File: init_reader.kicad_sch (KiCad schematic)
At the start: 3 parts, among them U1 LCD_16x4, U2 MAX232

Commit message: update schematics
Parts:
- added BT1: Battery, Battery:BatteryHolder_MPD_BA9VPC_1xPP3, symbol Device:Battery
- added C1, C2, C3, C4: 10uF, Capacitor_THT:CP_Radial_D5.0mm_P2.50mm, symbol Device:C_Polarized
- added J1: DE9_Pins, Connector_Dsub:DSUB-9_Pins_Horizontal_P2.77x2.54mm_EdgePinOffset9.40mm, symbol Connector:DE9_Pins
- added R1: R, Resistor_THT:R_Axial_DIN0207_L6.3mm_D2.5mm_P7.62mm_Horizontal, symbol Device:R
- U1: footprint PCM_SL_Breakout_Boards:LCD-16X4 -> 0_moje:AC-164A
- U2: footprint (none) -> Package_DIP:DIP-16_W7.62mm
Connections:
- net +5V: now also U1.15 (LED_A), U1.2 (VDD), U2.16 (VCC), C3.2
- net GND: now also A1.13 (GND), A1.18 (GND), A1.23 (GND), A1.28 (GND), A1.3 (GND), A1.38 (GND), A1.8 (GND), U1.1 (VSS), U1.16 (LED_K), U1.5 (RW), U2.15 (GND), C4.1, J1.5, R1.2
- net DB4: now reaches U1.11 (DB4)
- net DB4: now also A1.25 (GPIO19)
- net DB5: now reaches U1.12 (DB5)
- net DB5: now also A1.24 (GPIO18)
- net DB6: now reaches U1.13 (DB6)
- net DB6: now also A1.22 (GPIO17)
- net DB7: now reaches U1.14 (DB7)
- net DB7: now also A1.21 (GPIO16)
- net at U1.3 (VO): now also R1.1
- net RS: now reaches U1.4 (RS)
- net RS: now also A1.27 (GPIO21)
- net En: now reaches U1.6 (E)
- net En: now also A1.26 (GPIO20)
- net at U2.1 (C1+): now also C1.1
- net T1OUT: now reaches U2.11 (T1IN)
- net R1OUT: now reaches U2.12 (R1OUT)
- net R1IN: now reaches U2.13 (R1IN)
- net R1IN: now also J1.3
- net T1IN: now reaches U2.14 (T1OUT)
- net T1IN: now also J1.2
- net at U2.2 (VS+): now also C3.1
- net at U2.3 (C1-): now also C1.2
- net at U2.4 (C2+): now also C2.1
- net at U2.5 (C2-): now also C2.2
- net at U2.6 (VS-): now also C4.2
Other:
- moved on the sheet: U1

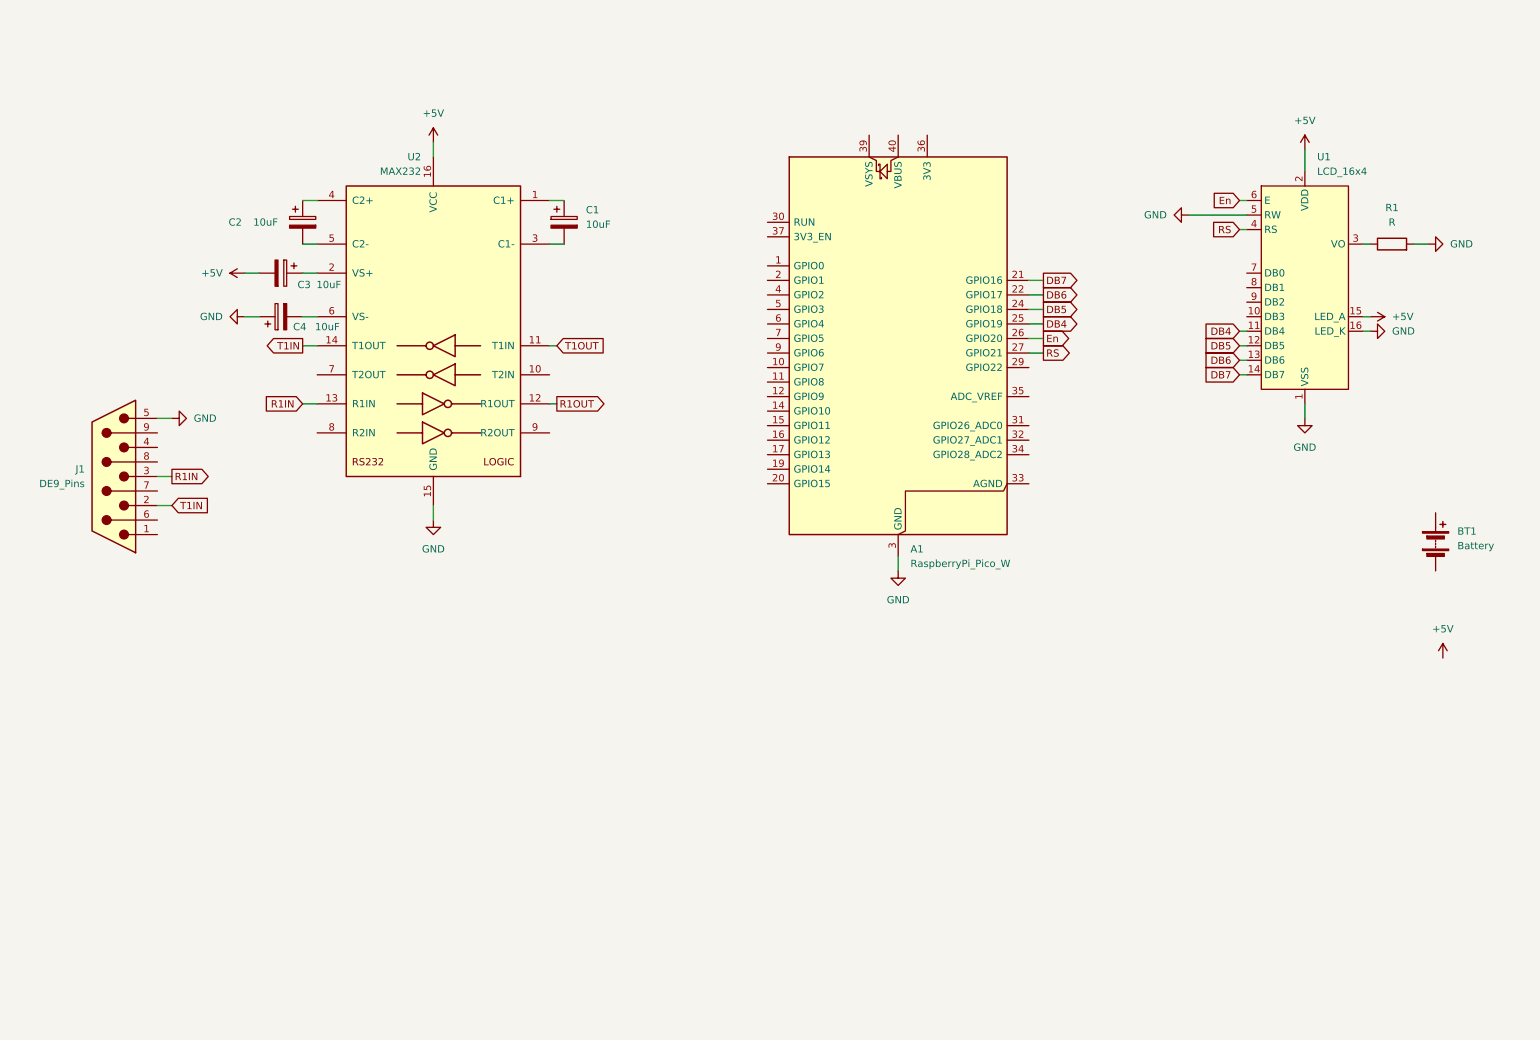
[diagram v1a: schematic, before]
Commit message: add all components - basic circuit
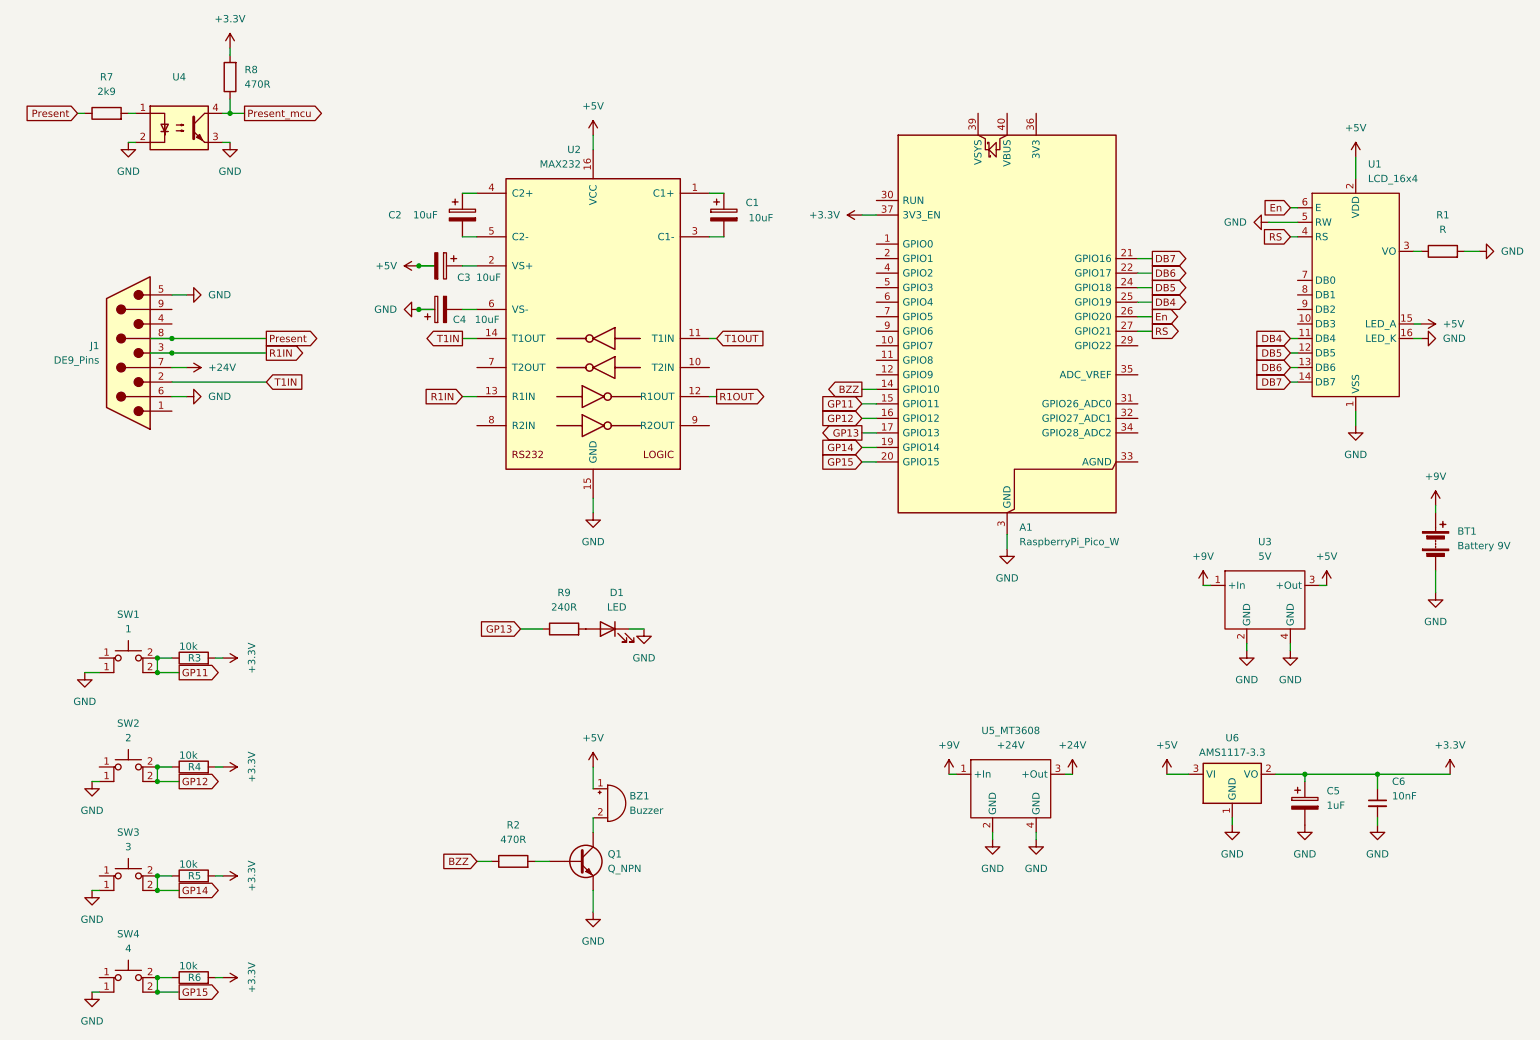
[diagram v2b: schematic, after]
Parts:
- added BZ1: Buzzer, Buzzer_Beeper:Buzzer_12x9.5RM7.6, symbol 00_my_basic:Buzzer
- added C5: 1uF, Capacitor_THT:CP_Radial_D5.0mm_P2.50mm, symbol Device:C_Polarized
- added C6: 10nF, PCM_SparkFun-Capacitor:C_0603_1608Metric, symbol 00_my_basic:C
- added D1: LED, LED_THT:LED_D3.0mm, symbol Device:LED
- added Q1: Q_NPN, Package_TO_SOT_THT:TO-92_Inline, symbol 00_my_basic:Q_NPN
- added R2, R8: 470R, Resistor_THT:R_Axial_DIN0207_L6.3mm_D2.5mm_P7.62mm_Horizontal, symbol Device:R
- added R3, R4, R5, R6: 10k, Resistor_THT:R_Axial_DIN0207_L6.3mm_D2.5mm_P7.62mm_Horizontal, symbol Device:R
- added R7: 2k9, Resistor_THT:R_Axial_DIN0207_L6.3mm_D2.5mm_P7.62mm_Horizontal, symbol Device:R
- added R9: 240R, Resistor_THT:R_Axial_DIN0207_L6.3mm_D2.5mm_P7.62mm_Horizontal, symbol Device:R
- added SW1: 1, Button_Switch_THT:SW_TH_Tactile_Omron_B3F-100x, symbol 00_my_basic:Switch 4 poly
- added SW2: 2, Button_Switch_THT:SW_TH_Tactile_Omron_B3F-100x, symbol 00_my_basic:Switch 4 poly
- added SW3: 3, Button_Switch_THT:SW_TH_Tactile_Omron_B3F-100x, symbol 00_my_basic:Switch 4 poly
- added SW4: 4, Button_Switch_THT:SW_TH_Tactile_Omron_B3F-100x, symbol 00_my_basic:Switch 4 poly
- added U3: 5V, 00_dc_dc:dc-dc-HW613, symbol 00_my_basic:DC/DC
- added U4: Optocoupler_DC_PhotoNPN_AKEC, OptoDevice:Vishay_CNY70, symbol Isolator:Optocoupler_DC_PhotoNPN_AKEC
- added U5_MT3608: +24V, 00_dc_dc:dc_dc_MT3608, symbol 00_my_basic:DC/DC
- added U6: AMS1117-3.3, Package_TO_SOT_SMD:SOT-223-3_TabPin2, symbol Regulator_Linear:AMS1117-3.3
- A1: footprint Module:RaspberryPi_Pico_W_SMD_HandSolder -> 00_ruzne:RaspberryPi_Pico_Common_THT
- BT1: value Battery -> Battery 9V
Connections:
- net +5V: now also BZ1.1 (+), U3.3 (+Out), U6.3 (VI)
- net GND: now also BT1.2 (-), J1.6, C5.2, C6.2, D1.1 (K), Q1.3 (E), SW1.1, SW2.1, SW3.1, SW4.1, U3.2 (GND), U3.4 (GND), U4.2, U4.3, U5_MT3608.2 (GND), U5_MT3608.4 (GND), U6.1 (GND)
- net +9V: now reaches BT1.1 (+)
- net +9V: now also U3.1 (+In), U5_MT3608.1 (+In)
- net +24V: now reaches J1.7
- net +24V: now also U5_MT3608.3 (+Out)
- net Present: now reaches J1.8
- net Present: now also R7.1
- net BZZ: now reaches A1.14 (GPIO10)
- net BZZ: now also R2.1
- net GP11: now reaches A1.15 (GPIO11)
- net GP11: now also R3.1, SW1.2
- net GP12: now reaches A1.16 (GPIO12)
- net GP12: now also R4.1, SW2.2
- net GP13: now reaches A1.17 (GPIO13)
- net GP13: now also R9.1
- net GP14: now reaches A1.19 (GPIO14)
- net GP14: now also R5.1, SW3.2
- net GP15: now reaches A1.20 (GPIO15)
- net GP15: now also R6.1, SW4.2
- net +3.3V: now reaches A1.37 (3V3_EN)
- net +3.3V: now also C5.1, C6.1, R3.2, R4.2, R5.2, R6.2, R8.2, U6.2 (VO)
- new net: Q1.2 (B), R2.2
- new net: R7.2, U4.1
- new net: D1.2 (A), R9.2
- new net: BZ1.2 (-), Q1.1 (C)
- new net Present_mcu: R8.1, U4.4
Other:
- moved on the sheet: A1, C1, C2, C3, C4, J1, R1, U1, U2

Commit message: update all
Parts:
- U4: footprint OptoDevice:Vishay_CNY70 -> Package_DIP:DIP-4_W7.62mm
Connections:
- net Present: now also J1.1; no longer J1.8
- net Present_mcu: now also A1.9 (GPIO6)
- net R1IN: now also J1.2; no longer J1.3
- net R1OUT: now also A1.2 (GPIO1)
- net T1IN: now also J1.3; no longer J1.2
- net T1OUT: now also A1.1 (GPIO0)
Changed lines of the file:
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@@
+	)
+	(junction
+		(at 45.72 76.2)
+		(diameter 0)
+		(color 0 0 0 0)
 	)
 	(junction
@@
 	)
 	(junction
-		(at 45.72 71.12)
-		(diameter 0)
-		(color 0 0 0 0)
-	)
-	(junction
-		(at 45.72 68.58)
-		(diameter 0)
-		(color 0 0 0 0)
-	)
-	(junction
 		(at 43.18 162.56)
 		(diameter 0)
@@
 	(wire
 		(pts
-			(xy 62.23 71.12) (xy 45.72 71.12)
-		)
-		(stroke
-			(width 0)
-			(type default)
-		)
-	)
-	(wire
-		(pts
 			(xy 96.52 78.74) (xy 99.06 78.74)
 		)
@@
 	(wire
 		(pts
-			(xy 41.91 71.12) (xy 45.72 71.12)
-		)
-		(stroke
-			(width 0)
-			(type default)
-		)
-	)
-	(wire
-		(pts
 			(xy 43.18 127) (xy 46.99 127)
 		)
@@
 	(wire
 		(pts
-			(xy 45.72 68.58) (xy 62.23 68.58)
-		)
-		(stroke
-			(width 0)
-			(type default)
-		)
-	)
-	(wire
-		(pts
 			(xy 31.75 182.88) (xy 33.02 182.88)
 		)
@@
 	(wire
 		(pts
+			(xy 167.64 54.61) (xy 168.91 54.61)
+		)
+		(stroke
+			(width 0)
+			(type default)
+		)
+	)
+	(wire
+		(pts
 			(xy 43.18 180.34) (xy 43.18 182.88)
 		)
@@
 	(wire
 		(pts
+			(xy 45.72 81.28) (xy 63.5 81.28)
+		)
+		(stroke
+			(width 0)
+			(type default)
+		)
+	)
+	(wire
+		(pts
 			(xy 166.37 82.55) (xy 168.91 82.55)
 		)
@@
 	(wire
 		(pts
+			(xy 167.64 67.31) (xy 168.91 67.31)
+		)
+		(stroke
+			(width 0)
+			(type default)
+		)
+	)
+	(wire
+		(pts
 			(xy 48.26 60.96) (xy 45.72 60.96)
 		)
@@
 	(wire
 		(pts
+			(xy 44.45 76.2) (xy 45.72 76.2)
+		)
+		(stroke
+			(width 0)
+			(type default)
+		)
+	)
+	(wire
+		(pts
+			(xy 45.72 71.12) (xy 63.5 71.12)
+		)
+		(stroke
+			(width 0)
+			(type default)
+		)
+	)
+	(wire
+		(pts
 			(xy 43.18 124.46) (xy 43.18 127)
 		)
@@
 	(wire
 		(pts
-			(xy 41.91 68.58) (xy 45.72 68.58)
-		)
-		(stroke
-			(width 0)
-			(type default)
-		)
-	)
-	(wire
-		(pts
-			(xy 62.23 76.2) (xy 45.72 76.2)
-		)
-		(stroke
-			(width 0)
-			(type default)
-		)
-	)
-	(wire
-		(pts
 			(xy 31.75 165.1) (xy 33.02 165.1)
 		)
@@
 	(wire
 		(pts
+			(xy 45.72 76.2) (xy 63.5 76.2)
+		)
+		(stroke
+			(width 0)
+			(type default)
+		)
+	)
+	(wire
+		(pts
 			(xy 166.37 90.17) (xy 168.91 90.17)
 		)
@@
 		(pts
 			(xy 99.06 160.02) (xy 101.6 160.02)
+		)
+		(stroke
+			(width 0)
+			(type default)
+		)
+	)
+	(wire
+		(pts
+			(xy 167.64 52.07) (xy 168.91 52.07)
 		)
 		(stroke
@@
 		)
 	)
+	(global_label "Present_mcu"
+		(shape input)
+		(at 167.64 67.31 180)
+		(fields_autoplaced yes)
+		(effects
+			(font
+				(size 1.27 1.27)
+			)
+			(justify right)
+		)
+		(property "Intersheetrefs" "${INTERSHEET_REFS}"
+			(at 152.6201 67.31 0)
+			(effects
+				(font
+					(size 1.27 1.27)
+				)
+				(justify right)
+				(hide yes)
+			)
+		)
+	)
 	(global_label "BZZ"
 		(shape input)
@@
 	(global_label "Present"
 		(shape output)
-		(at 62.23 68.58 0)
+		(at 63.5 81.28 0)
 		(fields_autoplaced yes)
 		(effects
@@
 		)
 		(property "Intersheetrefs" "${INTERSHEET_REFS}"
-			(at 72.3514 68.58 0)
+			(at 73.6214 81.28 0)
 			(effects
 				(font
@@
 		)
 	)
+	(global_label "T1OUT"
+		(shape output)
+		(at 167.64 52.07 180)
+		(fields_autoplaced yes)
+		(effects
+			(font
+				(size 1.27 1.27)
+			)
+			(justify right)
+		)
+		(property "Intersheetrefs" "${INTERSHEET_REFS}"
+			(at 158.8491 52.07 0)
+			(effects
+				(font
+					(size 1.27 1.27)
+				)
+				(justify right)
+				(hide yes)
+			)
+		)
+	)
 	(global_label "R1IN"
 		(shape output)
-		(at 62.23 71.12 0)
+		(at 63.5 76.2 0)
 		(fields_autoplaced yes)
 		(effects
@@
 		)
 		(property "Intersheetrefs" "${INTERSHEET_REFS}"
-			(at 69.63 71.12 0)
+			(at 70.9 76.2 0)
 			(effects
 				(font
@@
 		)
 	)
+	(global_label "R1OUT"
+		(shape input)
+		(at 167.64 54.61 180)
+		(fields_autoplaced yes)
+		(effects
+			(font
+				(size 1.27 1.27)
+			)
+			(justify right)
+		)
+		(property "Intersheetrefs" "${INTERSHEET_REFS}"
+			(at 158.5467 54.61 0)
+			(effects
+				(font
+					(size 1.27 1.27)
+				)
+				(justify right)
+				(hide yes)
+			)
+		)
+	)
 	(global_label "T1IN"
 		(shape output)
@@
 	(global_label "T1IN"
 		(shape input)
-		(at 62.23 76.2 0)
+		(at 63.5 71.12 0)
 		(fields_autoplaced yes)
 		(effects
@@
 		)
 		(property "Intersheetrefs" "${INTERSHEET_REFS}"
-			(at 69.3276 76.2 0)
+			(at 70.5976 71.12 0)
 			(effects
 				(font
@@
 			)
 		)
-		(property "Footprint" "OptoDevice:Vishay_CNY70"
+		(property "Footprint" "Package_DIP:DIP-4_W7.62mm"
 			(at 41.91 36.83 0)
 			(effects
